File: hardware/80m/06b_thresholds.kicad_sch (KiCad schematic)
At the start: 9 parts

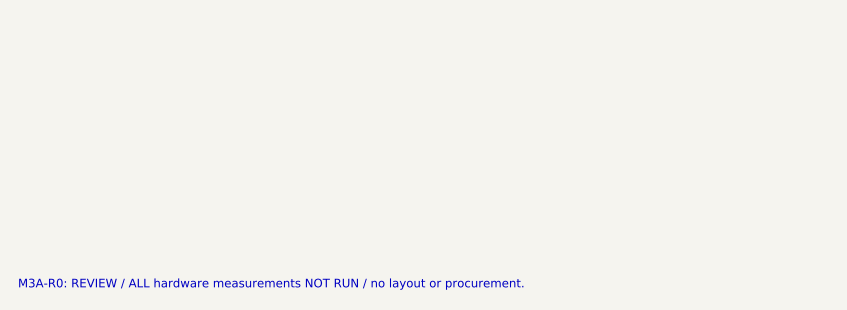
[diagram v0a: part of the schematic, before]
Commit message: Correct RF80 timer polarities and arming logic for M3A-R1 review
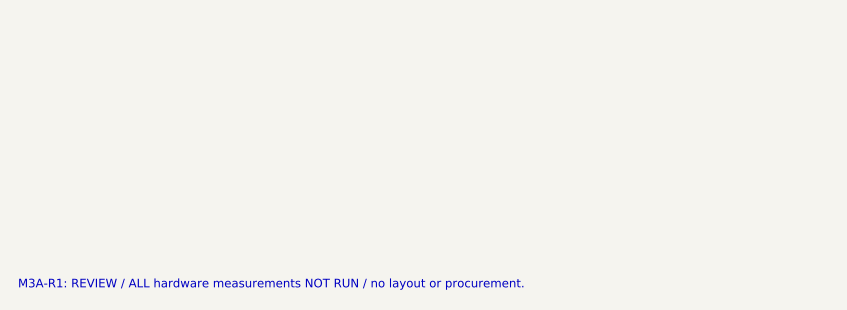
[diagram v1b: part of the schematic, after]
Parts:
- R317, R318, R326, R327, R328, R329: Population BOTH -> NORMAL
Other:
- note added: "M3A-R1: REVIEW / ALL hardware measurements NOT RUN / no layout or procurement."
- note removed: "M3A-R0: REVIEW / ALL hardware measurements NOT RUN / no layout or procurement."

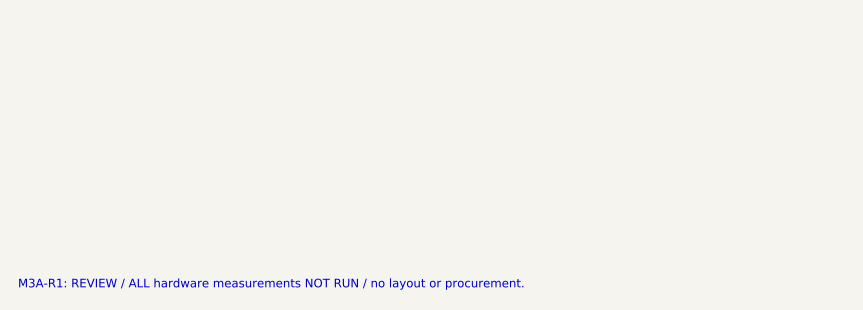
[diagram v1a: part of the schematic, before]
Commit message: Preserve M3B-E1 evaluation PCB before independent-review corrections
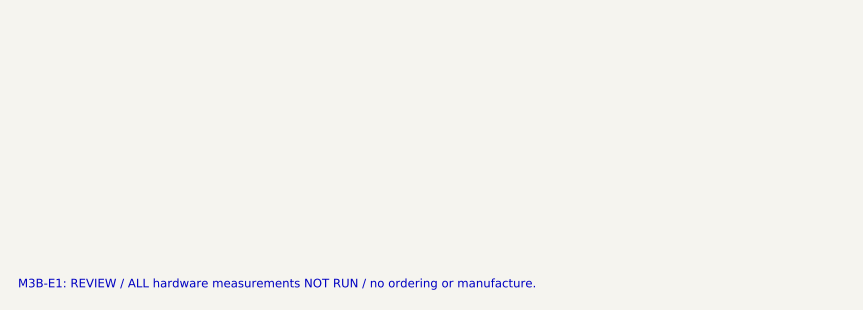
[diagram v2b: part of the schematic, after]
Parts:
- R316, R318, R327, R329: Engineering_Note Dated M2 distributor observation; no fresh basket verificat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 -> (none)
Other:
- note added: "M3B-E1: REVIEW / ALL hardware measurements NOT RUN / no ordering or manufacture."
- note removed: "M3A-R1: REVIEW / ALL hardware measurements NOT RUN / no layout or procurement."

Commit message: Correct RF80 M3B-E2 physical pinouts and audit manufacturing readiness
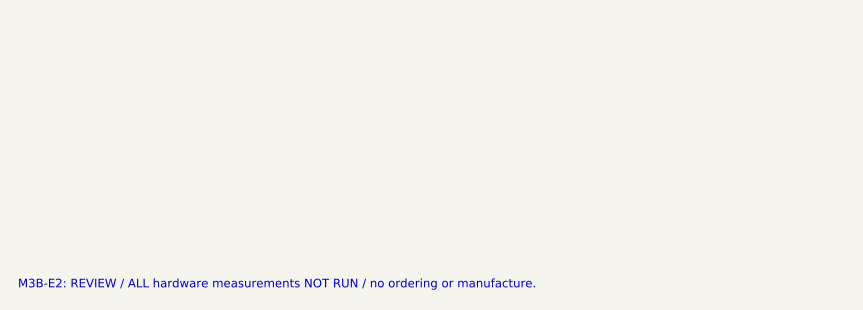
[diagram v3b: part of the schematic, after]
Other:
- note added: "M3B-E2: REVIEW / ALL hardware measurements NOT RUN / no ordering or manufacture."
- note removed: "M3B-E1: REVIEW / ALL hardware measurements NOT RUN / no ordering or manufacture."
